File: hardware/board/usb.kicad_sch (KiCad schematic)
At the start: 5 parts, among them J8 USB_B_Micro, P1 USB_C_Plug_USB2.0, U10 AP22653W6, U9 FSUSB42MX

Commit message: finish usb?
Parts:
- added C62: 0.1uF, Capacitor_SMD:C_0805_2012Metric, symbol Device:C_Small
- added C63: 10uF, Capacitor_SMD:C_0805_2012Metric, symbol Device:C_Small
- added R32: 49.9k @ 1%, symbol Device:R_Small
- added R33: 10k, symbol Device:R_Small
- added R34, R35: 56k, symbol Device:R_Small
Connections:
- net GND: now also J8.5 (GND), J8.SH (Shield), P1.A1 (GND), P1.A12 (GND), P1.B1 (GND), P1.B12 (GND), P1.SH (SHIELD), U10.2 (GND), C62.2, C63.2, R32.2
- net at U10.1 (IN): now also C62.1, C63.1
- net USBH_EN: now reaches U10.3 (EN)
- net USBH_~{FAULT}: now reaches U10.4 (nFault)
- net USBH_~{FAULT}: now also R33.2
- net at U10.5 (ILIM): now also R32.1
- net at U10.6 (OUT): now also P1.A4 (VBUS), P1.A9 (VBUS), P1.B4 (VBUS), P1.B9 (VBUS)
- net at P1.A5 (CC): now also R34.2
- net at P1.B5 (VCONN): now also R35.1
- new net +5V: R33.1, R34.1, R35.2
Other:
- moved on the sheet: J8, P1, R31, U10, U9

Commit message: finish assignment
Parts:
- J8: footprint (none) -> CM4IO:USB_Micro-B_EDAC_UCON00686
- R31, R32, R33, R34, R35: footprint (none) -> Resistor_SMD:R_0805_2012Metric
- U9: footprint (none) -> Package_SO:MSOP-10_3x3mm_P0.5mm
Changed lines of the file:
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@@
 			)
 		)
-		(property "Footprint" ""
+		(property "Footprint" "Resistor_SMD:R_0805_2012Metric"
 			(at 184.15 58.42 0)
 			(hide yes)
@@
 			)
 		)
-		(property "Footprint" ""
+		(property "Footprint" "Resistor_SMD:R_0805_2012Metric"
 			(at 184.15 60.96 0)
 			(hide yes)
@@
 			)
 		)
-		(property "Footprint" ""
+		(property "Footprint" "CM4IO:USB_Micro-B_EDAC_UCON00686"
 			(at 85.09 110.49 0)
 			(hide yes)
@@
 			)
 		)
-		(property "Footprint" ""
+		(property "Footprint" "Package_SO:MSOP-10_3x3mm_P0.5mm"
 			(at 148.59 130.81 0)
 			(hide yes)
@@
 			)
 		)
-		(property "Footprint" ""
+		(property "Footprint" "Resistor_SMD:R_0805_2012Metric"
 			(at 69.85 67.31 0)
 			(hide yes)
@@
 			)
 		)
-		(property "Footprint" ""
+		(property "Footprint" "Resistor_SMD:R_0805_2012Metric"
 			(at 167.64 110.49 0)
 			(hide yes)
@@
 			)
 		)
-		(property "Footprint" ""
+		(property "Footprint" "Resistor_SMD:R_0805_2012Metric"
 			(at 120.65 60.96 0)
 			(hide yes)

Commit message: connecting main
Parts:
- added C4: 1uF, Capacitor_SMD:C_0805_2012Metric, symbol Device:C_Small
- added C60: 3.3nF, Capacitor_SMD:C_0805_2012Metric, symbol Device:C_Small
- added C7: 0.1uF, Capacitor_SMD:C_0805_2012Metric, symbol Device:C_Small
- added J1: USB_C_Receptacle_PowerOnly_6P, Connector_USB:USB_C_Receptacle_HRO_TYPE-C-31-M-12, symbol Connector:USB_C_Receptacle_PowerOnly_6P
- added R1, R4: 5.1k, Resistor_SMD:R_0805_2012Metric, symbol Device:R_Small
- added R29: 681 @ 1%, Resistor_SMD:R_0805_2012Metric, symbol Device:R_Small
- added R30: 10k, Resistor_SMD:R_0805_2012Metric, symbol Device:R_Small
- added R5: 1M, Resistor_SMD:R_0805_2012Metric, symbol Device:R_Small
- added R6: 390k, Resistor_SMD:R_0805_2012Metric, symbol Device:R_Small
- added U1: TPS259531DSGR, ledaw:SON50P200X200X80-9N, symbol TPS259531DSGR:TPS259531DSGR
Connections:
- net +3V3: now also R30.1
- net +5V: now also C4.1, U1.5 (OUT)
- net GND: now also C4.2, C60.2, C7.2, J1.A12 (GND), J1.B12 (GND), J1.SH (SHIELD), R1.2, R29.2, R4.2, R6.2, U1.8 (GND), U1.9 (GND)
- new net: C7.1, J1.A9 (VBUS), J1.B9 (VBUS), R5.1, U1.3 (IN), U1.4 (IN)
- new net: R5.2, R6.1, U1.2 (EN/UVLO)
- new net: C60.1, U1.1 (DVDT)
- new net: J1.A5 (CC1), R4.1
- new net: J1.B5 (CC2), R1.1
- new net FUSE_FAULT: R30.2, U1.6 (~{FLT})
- new net FUSE_ILM: R29.1, U1.7 (ILM)
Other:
- note added: "fault not that useful cuz we can't do anything when there's no power"

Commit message: wire evertying up
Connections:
- net FUSE_FAULT renamed FUSE_~{FLT}
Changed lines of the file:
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@@
 		)
 	)
-	(label "FUSE_FAULT"
+	(label "FUSE_~{FLT}"
 		(at 142.24 162.56 180)
 		(effects

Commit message: reannoation with good linkage?
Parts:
- renumbered C63 to C501, C62 to C502, C7 to C503, C4 to C504, C60 to C505, J8 to J501, J1 to J502, P1 to P501, R34 to R501, R32 to R502, R35 to R503, R33 to R504, R31 to R505, R30 to R506, R5 to R507, R6 to R508, R29 to R509, R1 to R510, R4 to R511, U10 to U501, U9 to U502, U1 to U503

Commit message: some big tim routing
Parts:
- removed J502: USB_C_Receptacle_PowerOnly_6P, Connector_USB:USB_C_Receptacle_HRO_TYPE-C-31-M-12, symbol Connector:USB_C_Receptacle_PowerOnly_6P
- added J502: USB_C_Receptacle_PowerOnly_24P, Connector_USB:USB_C_Receptacle_HRO_TYPE-C-31-M-12, symbol Connector:USB_C_Receptacle_PowerOnly_24P
- renumbered R510 to R508, R511 to R509, R508 to R510, R509 to R511
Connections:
- net GND: now also J502.A1 (GND), J502.A12 (GND), J502.B1 (GND), J502.B12 (GND), J502.SH (SHIELD)
- net at C503.1, R507.1, U503.3 (IN)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: now also J502.A4 (VBUS), J502.A9 (VBUS), J502.B4 (VBUS), J502.B9 (VBUS)
- net at R509.1: now also J502.A5 (CC1)
- net at R508.1: now also J502.B5 (CC2)
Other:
- moved on the sheet: C503, C504, C505, R506, R507, R508, R509, R510, R511, U503

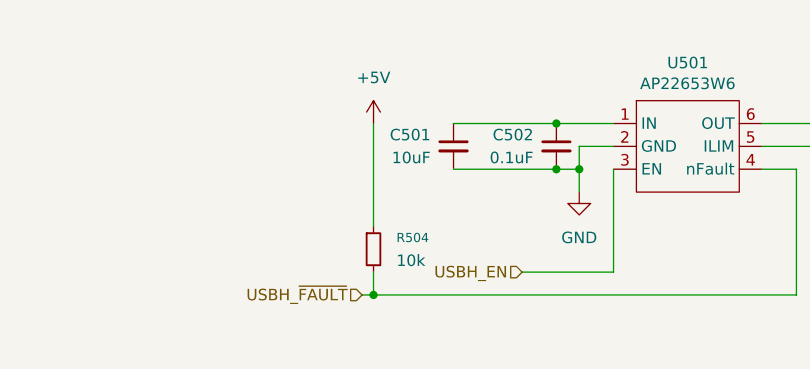
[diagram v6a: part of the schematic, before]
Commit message: forgot input to ILIM
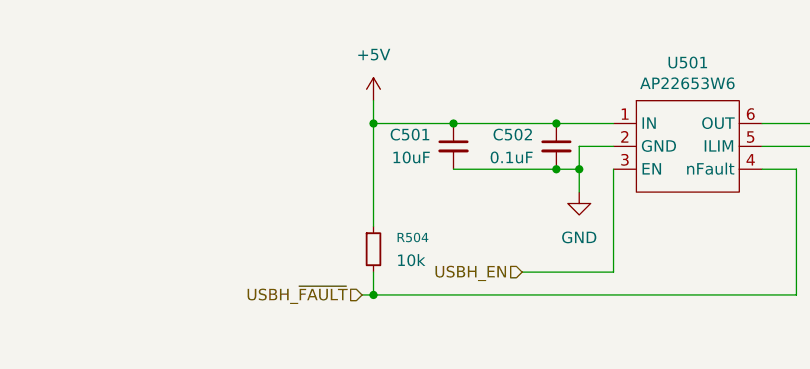
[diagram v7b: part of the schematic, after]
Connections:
- net +5V: now also C501.1, C502.1, U501.1 (IN)
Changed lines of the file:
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@@
+	)
+	(junction
+		(at 69.85 53.34)
+		(diameter 0)
+		(color 0 0 0 0)
 	)
 	(junction
@@
 	)
 	(junction
+		(at 78.74 53.34)
+		(diameter 0)
+		(color 0 0 0 0)
+	)
+	(junction
 		(at 204.47 91.44)
 		(diameter 0)
@@
 	(wire
 		(pts
+			(xy 69.85 50.8) (xy 69.85 53.34)
+		)
+		(stroke
+			(width 0)
+			(type default)
+		)
+	)
+	(wire
+		(pts
 			(xy 80.01 170.18) (xy 80.01 173.99)
+		)
+		(stroke
+			(width 0)
+			(type default)
+		)
+	)
+	(wire
+		(pts
+			(xy 69.85 53.34) (xy 78.74 53.34)
 		)
 		(stroke
@@
 	(symbol
 		(lib_id "power:+5V")
-		(at 69.85 53.34 0)
+		(at 69.85 50.8 0)
 		(unit 1)
 		(body_style 1)
@@
 		(fields_autoplaced yes)
 		(property "Reference" "#PWR0502"
-			(at 69.85 57.15 0)
+			(at 69.85 54.61 0)
 			(hide yes)
 			(show_name no)
@@
 		)
 		(property "Value" "+5V"
-			(at 69.85 48.26 0)
+			(at 69.85 45.72 0)
 			(show_name no)
 			(do_not_autoplace no)
@@
 		)
 		(property "Footprint" ""
-			(at 69.85 53.34 0)
+			(at 69.85 50.8 0)
 			(hide yes)
 			(show_name no)
@@
 		)
 		(property "Datasheet" ""
-			(at 69.85 53.34 0)
+			(at 69.85 50.8 0)
 			(hide yes)
 			(show_name no)
@@
 		)
 		(property "Description" "Power symbol creates a global label with name \"+5V\""
-			(at 69.85 53.34 0)
-			(hide yes)
-			(show_name no)
+			(at 69.85 50.8 0)
+			(hide yes)
+			(show_name no)

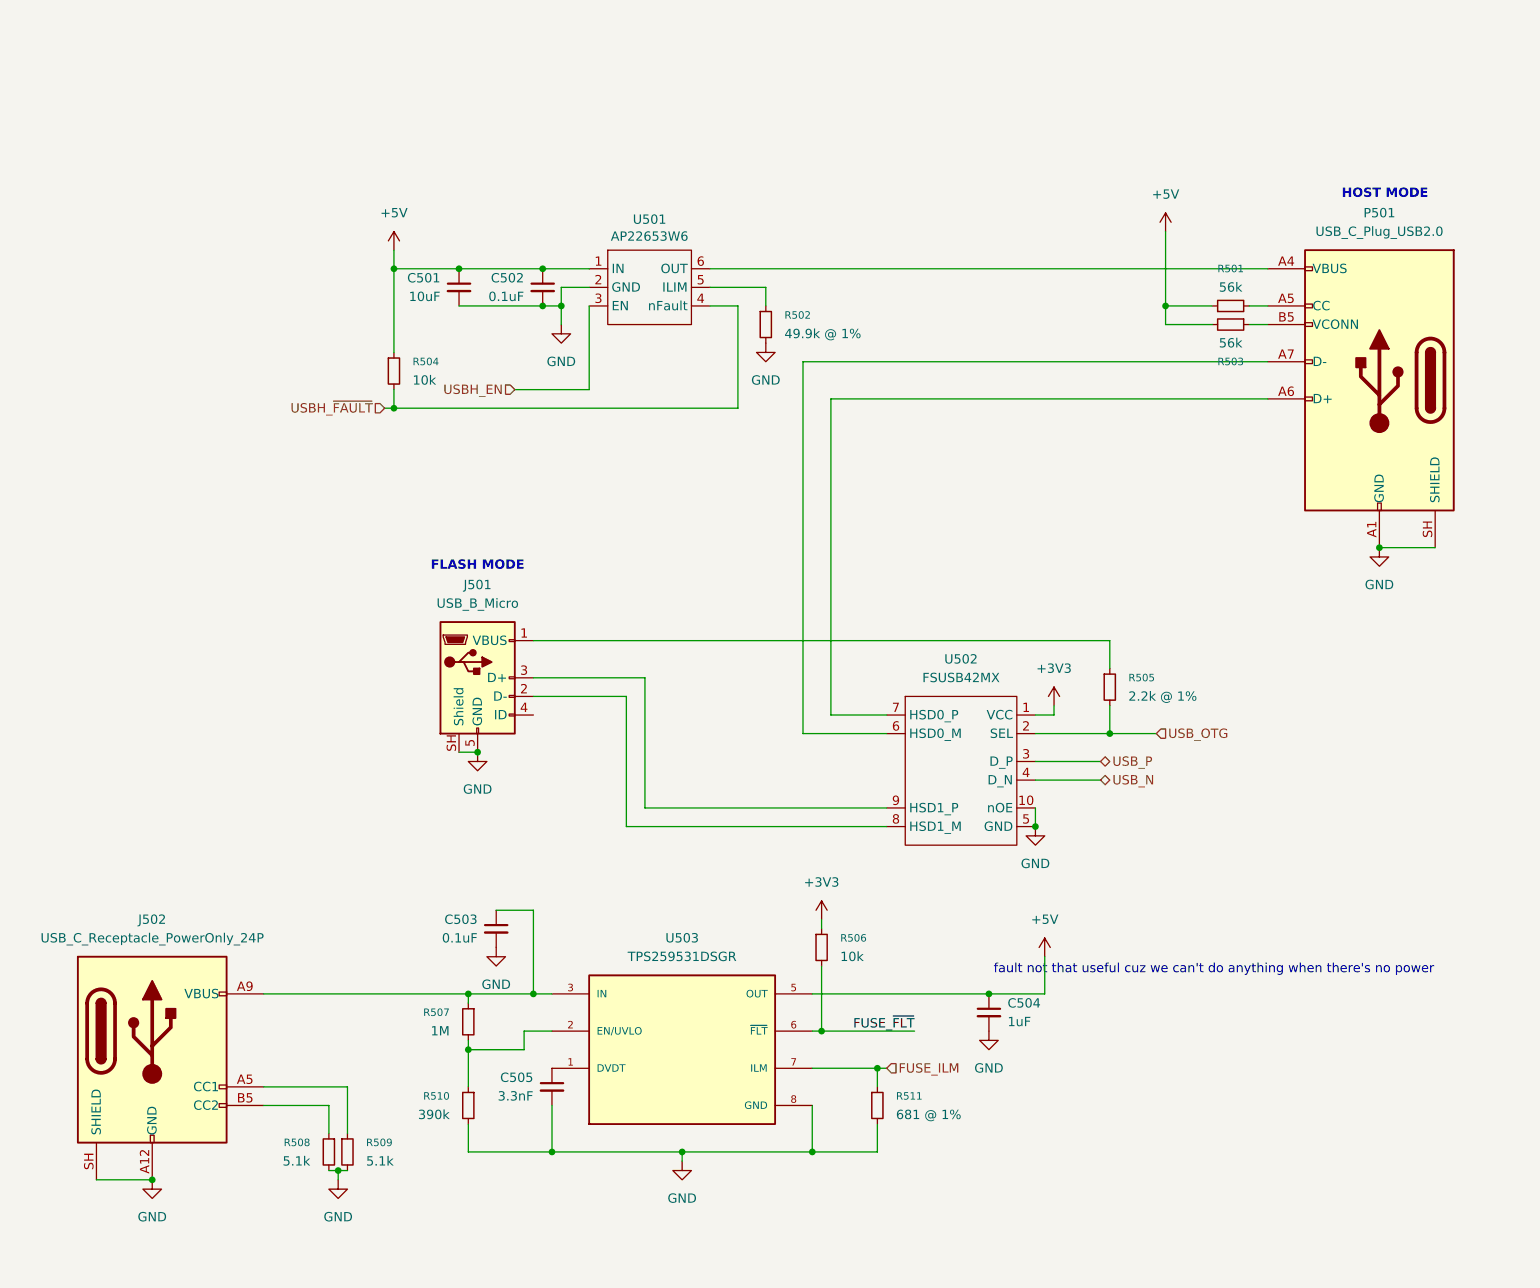
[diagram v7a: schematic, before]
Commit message: pre accidentally messed up the references
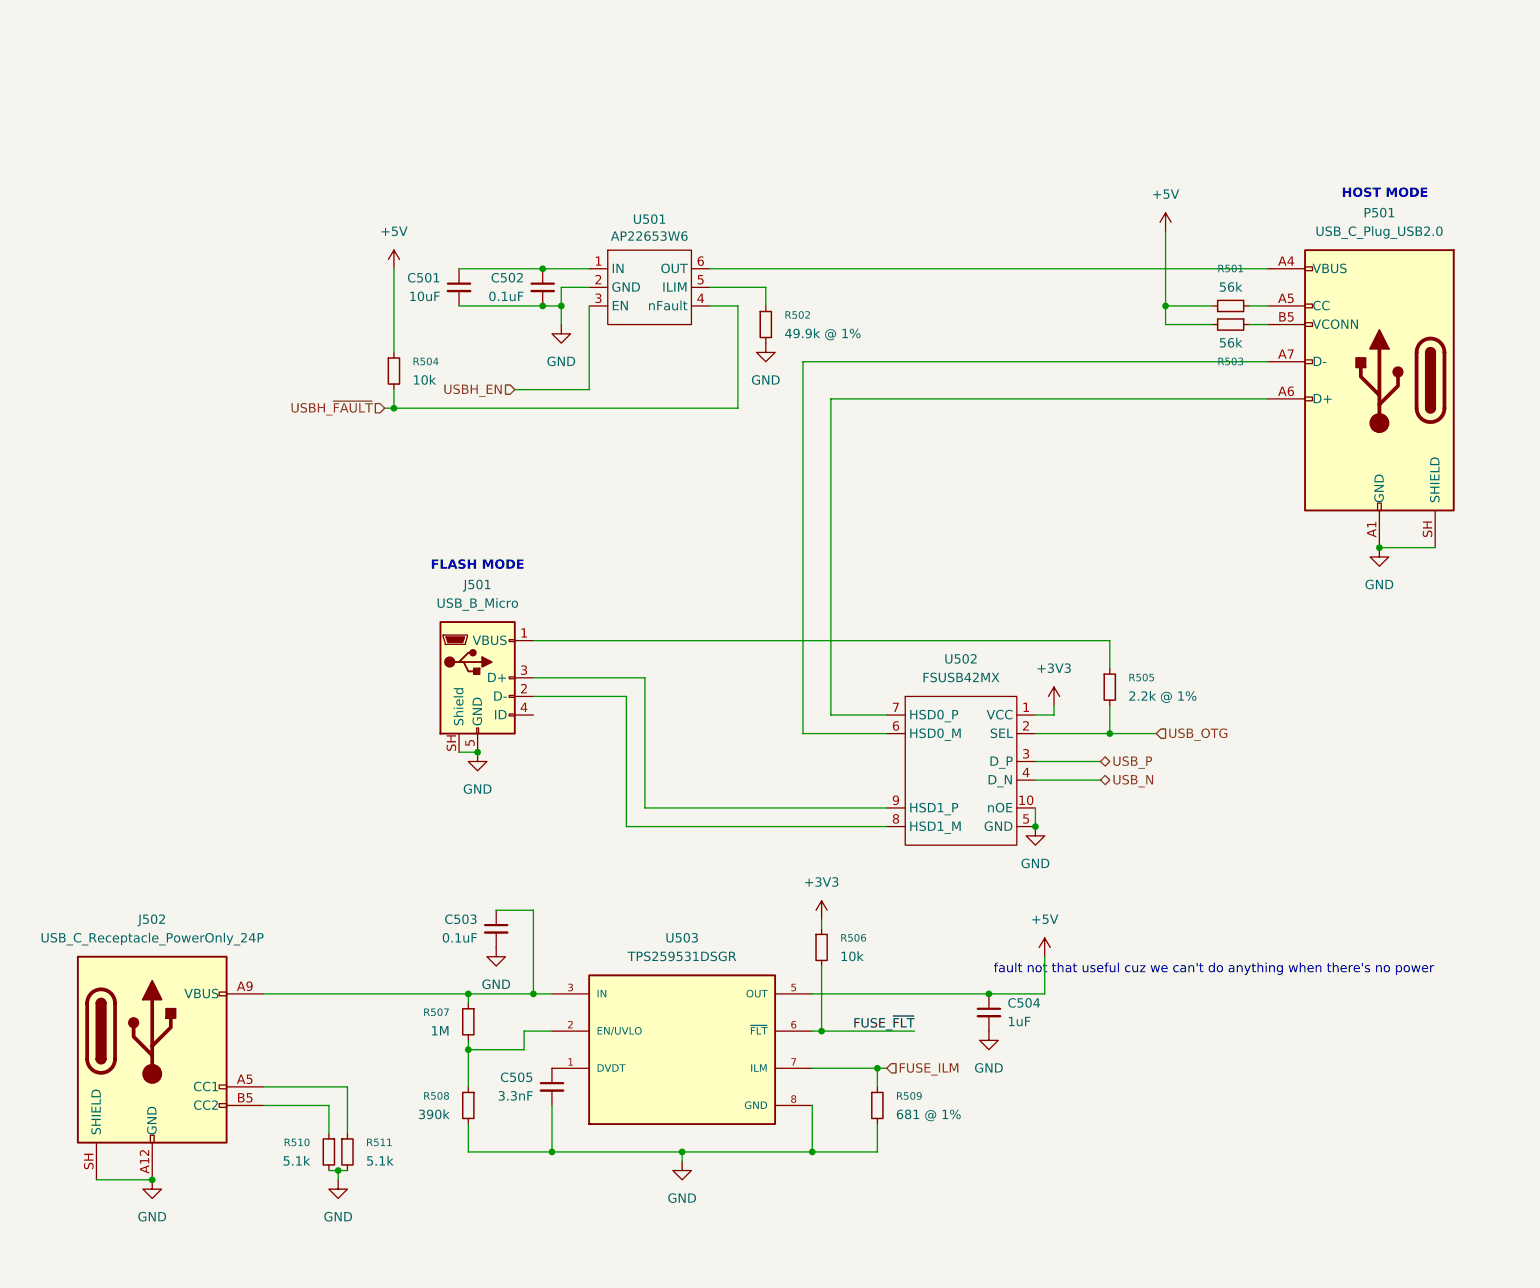
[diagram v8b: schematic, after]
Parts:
- renumbered R510 to R508, R511 to R509, R508 to R510, R509 to R511
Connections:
- net +5V: no longer C501.1, C502.1, U501.1 (IN)
- new net: C501.1, C502.1, U501.1 (IN)
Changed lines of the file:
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@@
 	)
 	(junction
-		(at 69.85 53.34)
-		(diameter 0)
-		(color 0 0 0 0)
-	)
-	(junction
 		(at 151.13 152.4)
 		(diameter 0)
@@
 	)
 	(junction
-		(at 78.74 53.34)
-		(diameter 0)
-		(color 0 0 0 0)
-	)
-	(junction
 		(at 204.47 91.44)
 		(diameter 0)
@@
 	(wire
 		(pts
-			(xy 69.85 50.8) (xy 69.85 53.34)
-		)
-		(stroke
-			(width 0)
-			(type default)
-		)
-	)
-	(wire
-		(pts
 			(xy 80.01 170.18) (xy 80.01 173.99)
 		)
@@
 	(wire
 		(pts
-			(xy 69.85 53.34) (xy 78.74 53.34)
-		)
-		(stroke
-			(width 0)
-			(type default)
-		)
-	)
-	(wire
-		(pts
 			(xy 167.64 116.84) (xy 173.99 116.84)
 		)
@@
 		(in_pos_files yes)
 		(dnp no)
-		(property "Reference" "R510"
+		(property "Reference" "R508"
 			(at 77.47 166.3699 0)
 			(show_name no)
@@
 			(project "board"
 				(path "/dd13fd41-39ab-4435-9074-5024f1786746/e77fa723-60b4-4aaf-b8c0-33f73a50a054"
-					(reference "R510")
+					(reference "R508")
 					(unit 1)
 				)
@@
 		(in_pos_files yes)
 		(dnp no)
-		(property "Reference" "R511"
+		(property "Reference" "R509"
 			(at 138.43 166.3699 0)
 			(show_name no)
@@
 			(project "board"
 				(path "/dd13fd41-39ab-4435-9074-5024f1786746/e77fa723-60b4-4aaf-b8c0-33f73a50a054"
-					(reference "R511")
+					(reference "R509")
 					(unit 1)
 				)
@@
 	(symbol
 		(lib_id "power:+5V")
-		(at 69.85 50.8 0)
+		(at 69.85 53.34 0)
 		(unit 1)
 		(body_style 1)
@@
 		(fields_autoplaced yes)
 		(property "Reference" "#PWR0502"
-			(at 69.85 54.61 0)
+			(at 69.85 57.15 0)
 			(hide yes)
 			(show_name no)
@@
 		)
 		(property "Value" "+5V"
-			(at 69.85 45.72 0)
+			(at 69.85 48.26 0)
 			(show_name no)
 			(do_not_autoplace no)
@@
 		)
 		(property "Footprint" ""
-			(at 69.85 50.8 0)
+			(at 69.85 53.34 0)
 			(hide yes)
 			(show_name no)
@@
 		)
 		(property "Datasheet" ""
-			(at 69.85 50.8 0)
+			(at 69.85 53.34 0)
 			(hide yes)
 			(show_name no)
@@
 		)
 		(property "Description" "Power symbol creates a global label with name \"+5V\""
-			(at 69.85 50.8 0)
+			(at 69.85 53.34 0)
 			(hide yes)
 			(show_name no)
@@
 		(dnp no)
 		(fields_autoplaced yes)
-		(property "Reference" "#PWR0513"
+		(property "Reference" "#PWR0515"
 			(at 62.23 184.15 0)
 			(hide yes)
@@
 			(project "board"
 				(path "/dd13fd41-39ab-4435-9074-5024f1786746/e77fa723-60b4-4aaf-b8c0-33f73a50a054"
-					(reference "#PWR0513")
+					(reference "#PWR0515")
 					(unit 1)
 				)
@@
 		(dnp no)
 		(fields_autoplaced yes)
-		(property "Reference" "#PWR0514"
+		(property "Reference" "#PWR0513"
 			(at 109.22 181.61 0)
 			(hide yes)
@@
 			(project "board"
 				(path "/dd13fd41-39ab-4435-9074-5024f1786746/e77fa723-60b4-4aaf-b8c0-33f73a50a054"
-					(reference "#PWR0514")
+					(reference "#PWR0513")
 					(unit 1)
 				)
@@
 		(dnp no)
 		(fields_autoplaced yes)
-		(property "Reference" "R509"
+		(property "Reference" "R511"
 			(at 66.04 172.7199 0)
 			(show_name no)
@@
 			(project "board"
 				(path "/dd13fd41-39ab-4435-9074-5024f1786746/e77fa723-60b4-4aaf-b8c0-33f73a50a054"
-					(reference "R509")
+					(reference "R511")
 					(unit 1)
 				)
@@
 		(dnp no)
 		(fields_autoplaced yes)
-		(property "Reference" "#PWR0515"
+		(property "Reference" "#PWR0514"
 			(at 36.83 184.15 0)
 			(hide yes)
@@
 			(project "board"
 				(path "/dd13fd41-39ab-4435-9074-5024f1786746/e77fa723-60b4-4aaf-b8c0-33f73a50a054"
-					(reference "#PWR0515")
+					(reference "#PWR0514")
 					(unit 1)
 				)
@@
 		(in_pos_files yes)
 		(dnp no)
-		(property "Reference" "R508"
+		(property "Reference" "R510"
 			(at 58.42 172.7199 0)
 			(show_name no)
@@
 			(project "board"
 				(path "/dd13fd41-39ab-4435-9074-5024f1786746/e77fa723-60b4-4aaf-b8c0-33f73a50a054"
-					(reference "R508")
+					(reference "R510")
 					(unit 1)
 				)
